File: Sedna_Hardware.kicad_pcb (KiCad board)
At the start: 2 copper layers, 50 parts, among them J1 PJ-102A, J10 5-103634-2, J11 2-644488-2, J2 61201021721, J3 Conn_01x14, J4 0878340619, J5 2-644803-3, J6 2-644488-3, J7 1935161, J8 1935161, J9 2-644803-3, K1 ALDP105W, K2 ALDP105W, Q1 2N7000-D75Z, Q2 2N7000-D75Z, U1 LD1117V33, U2 ESP32-WROOM-32D-N16, U3 LM6511IMX/NOPB

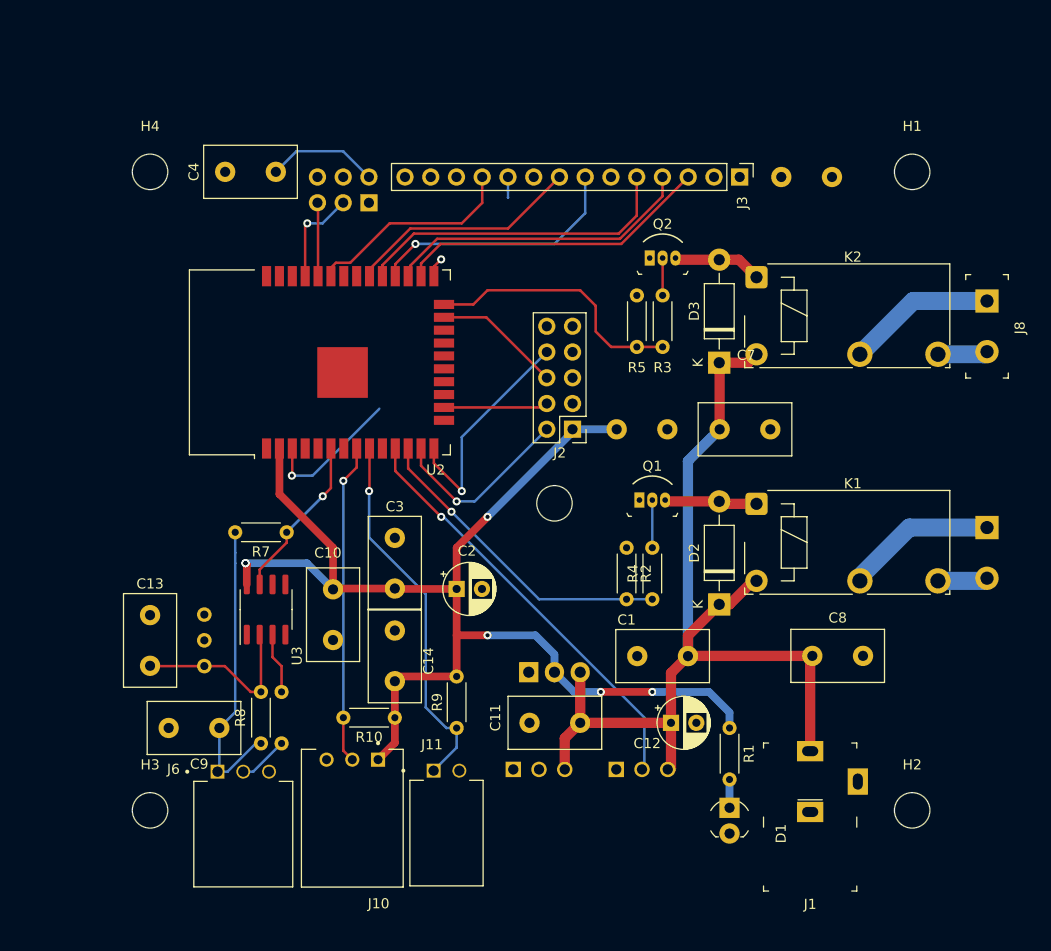
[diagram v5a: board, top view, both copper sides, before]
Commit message: finished track layout
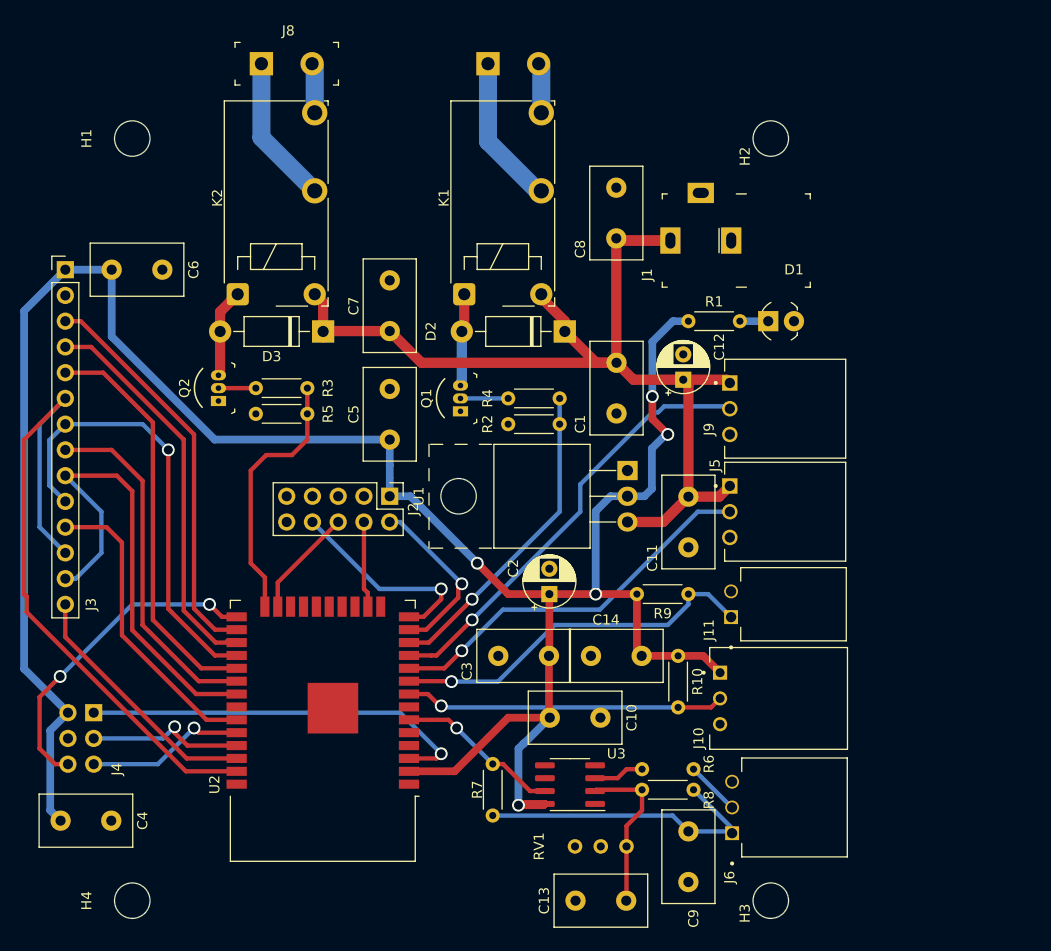
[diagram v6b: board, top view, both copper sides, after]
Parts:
- C5, C6, J5, J9, U1: moved to F.Cu
- moved H1 77.0 mm to (115.8, 67.3), turned to 90 degrees
- moved J8 75.3 mm to (128.6, 59.9), turned to 0 degrees
- moved H4 71.9 mm to (115.8, 142.5), turned to 90 degrees
- moved H2 67.7 mm to (178.8, 67.3), turned to 90 degrees
- moved C4 67.4 mm to (108.8, 134.6), turned to 0 degrees
- moved J7 67.2 mm to (150.9, 59.9), turned to 0 degrees
- moved J3 67.2 mm to (109.2, 80.3), turned to 0 degrees
- moved C6 66.7 mm to (113.8, 80.3)
- moved H3 61.9 mm to (178.8, 142.5), turned to 90 degrees
- moved J4 57.2 mm to (112.0, 124.0), turned to 180 degrees
- moved J1 54.5 mm to (171.9, 77.4), turned to -90 degrees
- moved C9 53.5 mm to (170.7, 140.7), turned to 90 degrees
- moved K2 51.2 mm to (126.2, 82.7), turned to 90 degrees
- moved J6 51.1 mm to (175.0, 135.9), turned to 90 degrees
- moved D1 50.9 mm to (181.1, 85.3), turned to 0 degrees
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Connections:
- J9 pad 1: GND -> +5V
- J9 pad 3: +5V -> GND
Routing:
- net +3V3: track 162.3 -> 259.7 mm, vias 6 -> 5
- net MOSI_LCD: track 0.00 -> 67.7 mm
- net MISO_LCD: track 0.00 -> 47.6 mm
- net LED_STRIP_CTRL: track 0.00 -> 38.1 mm, vias 0 -> 1
- net PROG_IO0: track 1.96 -> 33.2 mm, vias 1 -> 2
- net PROG_EN: track 14.1 -> 39.3 mm
- net TOUCH_IRQ: track 0.00 -> 25.1 mm
- net LCD_TOUCH_CLK: track 27.6 -> 44.5 mm
- net LCD_Brightness: track 23.2 -> 35.4 mm
- net TOUCH_CS: track 21.0 -> 31.0 mm
- net LCD_DC/RS: track 32.0 -> 41.5 mm
- net LCD_RESET: track 30.7 -> 40.0 mm
- net PROG_RXD0: track 7.27 -> 15.8 mm, vias 0 -> 1
- net LCD_CS: track 31.1 -> 39.6 mm
- net PROG_TXD0: track 9.69 -> 15.7 mm
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
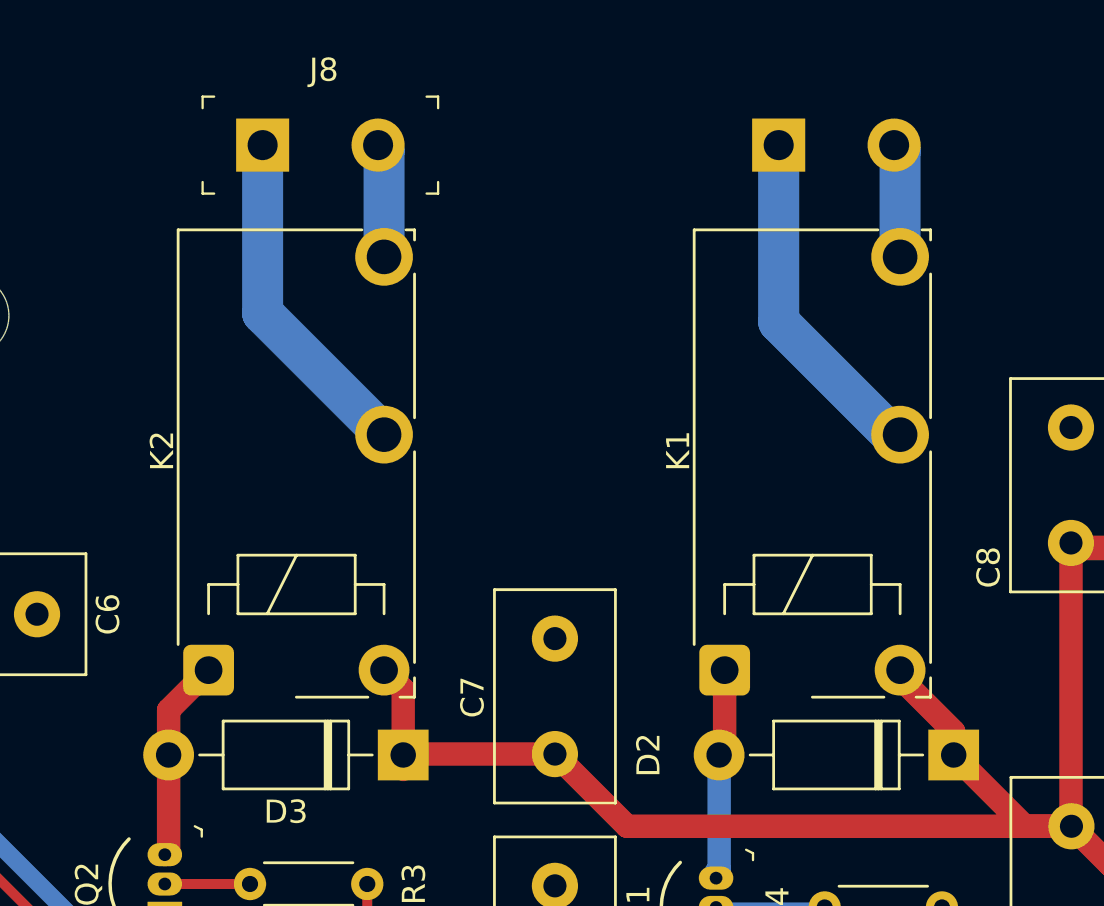
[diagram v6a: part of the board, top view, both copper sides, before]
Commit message: modified relay to correct footpring and symbol
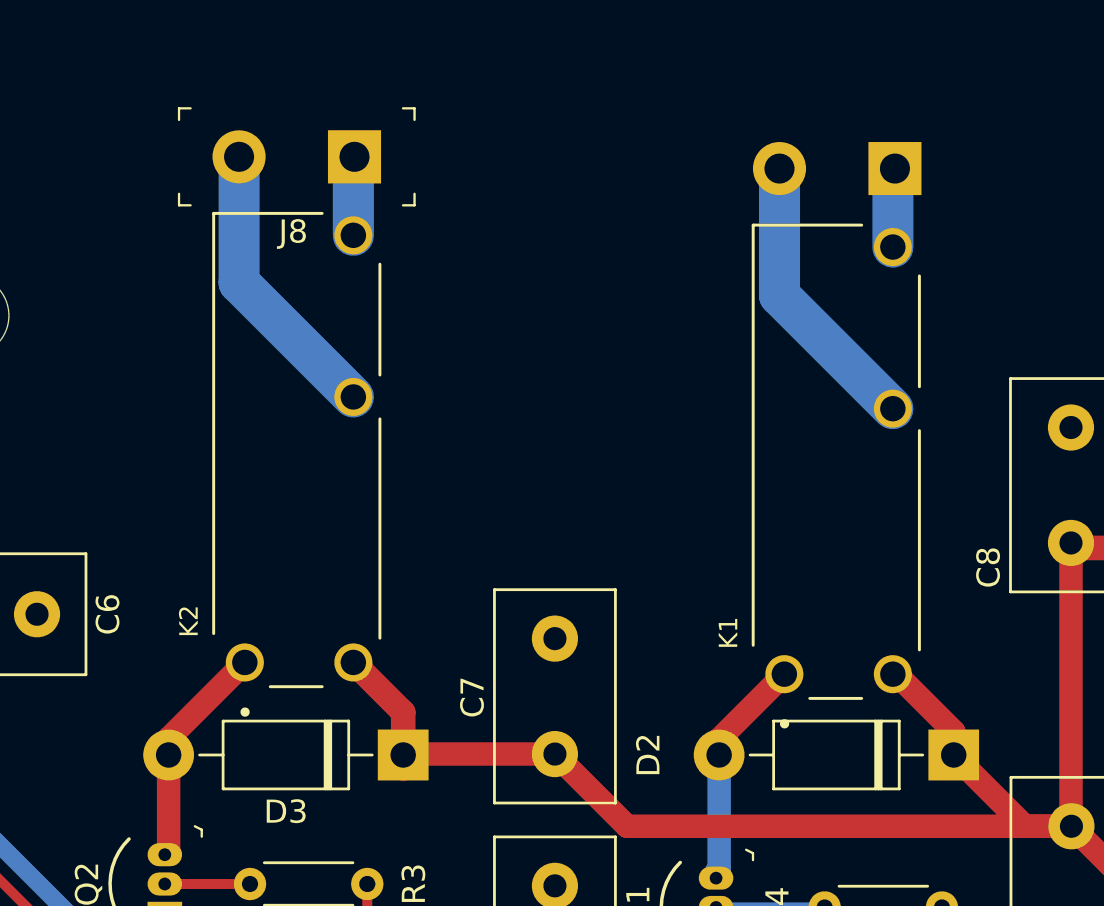
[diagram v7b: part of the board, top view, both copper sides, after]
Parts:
- J3: value Conn_01x14 -> PPTC141LFBN-RC
- K1, K2: footprint Relay_THT:Relay_SPST_TE_PCH-1xxx2M -> ALDP105W:RELAY_ALDP105W
- moved K2 10.3 mm to (130.0, 73.2)
- moved K1 10.2 mm to (153.4, 73.7)
- moved J7 5.14 mm to (156.0, 61.0), turned to 180 degrees
- moved J8 4.01 mm to (132.5, 60.5), turned to 180 degrees
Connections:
- C5 pad 1: +3V3 -> GND
- C5 pad 2: GND -> +3V3
- K1 pad 1: Net-(D2-Pad2) -> +5V
- K1 pad 2: Net-(J7-Pad1) -> Net-(D2-Pad2)
- K2 pad 1: Net-(D3-Pad2) -> +5V
- K2 pad 2: Net-(J8-Pad1) -> Net-(D3-Pad2)
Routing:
- net Net-(J7-Pad1): track 15.1 -> 3.44 mm
- net Net-(J8-Pad1): track 14.7 -> 3.42 mm
- net Net-(J8-Pad2): track 4.95 -> 12.5 mm
- net Net-(J7-Pad2): track 5.31 -> 12.4 mm
- net +5V: track 100.2 -> 101.4 mm
- net Net-(D3-Pad2): track 8.78 -> 9.76 mm
- net Net-(D2-Pad2): track 9.56 -> 10.1 mm

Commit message: added LCD & box drawings
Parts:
- moved J1 3.55 mm to (175.5, 77.3)
- moved H1 0.27 mm to (115.8, 67.1)
- moved H2 0.27 mm to (178.8, 67.1)
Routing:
- net +5V: track 101.4 -> 105.2 mm
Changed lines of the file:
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@@
   )
   (footprint "MountingHole:MountingHole_3.5mm" (layer "F.Cu")
-    (at 115.829 67.327755 90)
+    (at 115.829 67.056 90)
     (descr "Mounting Hole 3.5mm, no annular")
     (tags "mounting hole 3.5mm no annular")
@@
   )
   (footprint "digikey-footprints:Barrel_Jack_5.5mmODx2.1mmID_PJ-102A" (layer "F.Cu")
-    (at 171.915 77.391 -90)
+    (at 175.466 77.258 -90)
     (property "Category" "Connectors, Interconnects")
     (property "DK_Datasheet_Link" "https://www.cui.com/product/resource/digikeypdf/pj-102a.pdf")
@@
   )
   (footprint "MountingHole:MountingHole_3.5mm" (layer "F.Cu")
-    (at 178.821 67.327755 90)
+    (at 178.821 67.056 90)
     (descr "Mounting Hole 3.5mm, no annular")
     (tags "mounting hole 3.5mm no annular")
@@
     )
   )
+  (gr_line (start 101.092 148.336) (end 101.092 54.356) (layer "B.Cu") (width 0.2))
+  (gr_line (start 186.436 54.356) (end 186.436 148.336) (layer "B.Cu") (width 0.2))
+  (gr_line (start 186.436 148.336) (end 101.092 148.336) (layer "B.Cu") (width 0.2))
+  (gr_line (start 101.092 54.356) (end 186.436 54.356) (layer "B.Cu") (width 0.2))
   (gr_line (start 117.584238 133.604) (end 192.768238 133.604) (layer "F.CrtYd") (width 0.05))
-  (gr_line (start 115.829 67.327755) (end 178.821 67.327755) (layer "User.2") (width 0.15))
+  (gr_line (start 115.824 67.056) (end 115.824 54.356) (layer "User.2") (width 0.15))
+  (gr_line (start 178.821 67.056) (end 186.436 67.056) (layer "User.2") (width 0.15))
+  (gr_line (start 115.824 67.056) (end 178.821 67.056) (layer "User.2") (width 0.15))
   (gr_line (start 178.821 142.511755) (end 115.829 142.511755) (layer "User.2") (width 0.15))
-  (gr_line (start 178.821 67.327755) (end 178.821 142.511755) (layer "User.2") (width 0.15))
-  (gr_line (start 115.829 142.511755) (end 115.829 67.327755) (layer "User.2") (width 0.15))
-  (gr_line (start 33.02 55.88) (end 87.376 55.88) (layer "User.3") (width 0.15))
-  (gr_line (start 33.02 149.352) (end 33.02 55.88) (layer "User.3") (width 0.15))
-  (gr_line (start 87.376 55.88) (end 87.376 149.352) (layer "User.3") (width 0.15))
-  (gr_line (start 87.376 149.352) (end 33.02 149.352) (layer "User.3") (width 0.15))
+  (gr_line (start 178.821 67.056) (end 178.821 142.511755) (layer "User.2") (width 0.15))
+  (gr_line (start 115.829 142.511755) (end 115.824 67.056) (layer "User.2") (width 0.15))
+  (gr_line (start 115.824 67.056) (end 101.092 67.056) (layer "User.2") (width 0.15))
+  (gr_line (start 120.904 54.356) (end 175.26 54.356) (layer "User.3") (width 0.15))
+  (gr_line (start 120.904 147.828) (end 120.904 54.356) (layer "User.3") (width 0.15))
+  (gr_line (start 175.26 54.356) (end 175.26 147.828) (layer "User.3") (width 0.15))
+  (gr_line (start 175.26 147.828) (end 120.904 147.828) (layer "User.3") (width 0.15))
   (gr_line (start 182.885 57.404) (end 103.129 57.404) (layer "User.4") (width 0.15))
   (gr_line (start 103.129 57.404) (end 103.383 146.812) (layer "User.4") (width 0.15))
@@
   (segment (start 156.075 82.685) (end 155.956 82.804) (width 0.762) (layer "F.Cu") (net 1))
   (segment (start 168.193 105.156) (end 164.683 105.156) (width 1.016) (layer "F.Cu") (net 1))
+  (segment (start 172.466 77.258) (end 163.663 77.258) (width 1.0668) (layer "F.Cu") (net 1))
   (segment (start 163.601 89.448) (end 161.589 89.448) (width 1.016) (layer "F.Cu") (net 1))
-  (segment (start 168.915 77.391) (end 163.796 77.391) (width 1.0668) (layer "F.Cu") (net 1))
   (segment (start 165.274113 91.121113) (end 170.185 91.121113) (width 1.016) (layer "F.Cu") (net 1))
   (segment (start 170.185 91.629113) (end 170.693 91.121113) (width 0.25) (layer "F.Cu") (net 1))
+  (segment (start 163.663 77.258) (end 163.581 77.176) (width 1.0668) (layer "F.Cu") (net 1))
   (segment (start 173.7245 102.656) (end 174.7805 101.6) (width 1.016) (layer "F.Cu") (net 1))
   (segment (start 134.657004 86.36) (end 134.657004 84.511004) (width 1.0668) (layer "F.Cu") (net 1))
@@
   (segment (start 141.229 86.32) (end 135.452 86.32) (width 1.016) (layer "F.Cu") (net 1))
   (segment (start 170.693 91.629113) (end 170.693 102.656) (width 1.016) (layer "F.Cu") (net 1))
-  (segment (start 163.581 77.176) (end 163.581 89.448) (width 1.016) (layer "F.Cu") (net 1))
+  (segment (start 163.581 89.428) (end 163.601 89.448) (width 0.4318) (layer "F.Cu") (net 1))
   (segment (start 170.185 91.121113) (end 174.461613 91.121113) (width 1.016) (layer "F.Cu") (net 1))
   (segment (start 134.657 87.115) (end 134.625 87.083) (width 0.762) (layer "F.Cu") (net 1))
@@
   (segment (start 155.961 82.804) (end 158.501 85.344) (width 1.016) (layer "F.Cu") (net 1))
   (segment (start 170.185 91.121113) (end 170.693 91.629113) (width 1.016) (layer "F.Cu") (net 1))
+  (segment (start 163.581 77.176) (end 163.581 89.428) (width 1.0668) (layer "F.Cu") (net 1))
   (segment (start 174.461613 91.121113) (end 174.7805 91.44) (width 1.016) (layer "F.Cu") (net 1))
   (segment (start 156.18 82.685) (end 156.075 82.685) (width 0.762) (layer "F.Cu") (net 1))
@@
   (segment (start 112.95864 90.424) (end 109.225 90.424) (width 0.4318) (layer "F.Cu") (net 15))
   (segment (start 122.644 119.591) (end 117.861 114.808) (width 0.4318) (layer "F.Cu") (net 15))
+  (segment (start 105.415 114.046) (end 105.415 96.774) (width 0.4318) (layer "F.Cu") (net 16))
+  (segment (start 121.12 129.751) (end 105.415 114.046) (width 0.4318) (layer "F.Cu") (net 16))
+  (segment (start 105.415 96.774) (end 109.225 92.964) (width 0.4318) (layer "F.Cu") (net 16))
   (segment (start 126.125 129.751) (end 121.12 129.751) (width 0.4318) (layer "F.Cu") (net 16))
-  (segment (start 121.12 129.751) (end 105.415 114.046) (width 0.4318) (layer "F.Cu") (net 16))
-  (segment (start 105.161 112.268) (end 105.161 97.028) (width 0.4318) (layer "F.Cu") (net 16))
-  (segment (start 105.161 97.028) (end 109.225 92.964) (width 0.4318) (layer "F.Cu") (net 16))
-  (segment (start 105.415 114.046) (end 105.415 112.522) (width 0.4318) (layer "F.Cu") (net 16))
-  (segment (start 105.415 112.522) (end 105.22498 112.33198) (width 0.4318) (layer "F.Cu") (net 16))
-  (segment (start 105.415 112.522) (end 105.161 112.268) (width 0.4318) (layer "F.Cu") (net 16))
   (segment (start 109.225 92.964) (end 106.686869 95.502131) (width 0.4318) (layer "B.Cu") (net 16))
   (segment (start 106.686869 105.665869) (end 109.225 108.204) (width 0.4318) (layer "B.Cu") (net 16))
